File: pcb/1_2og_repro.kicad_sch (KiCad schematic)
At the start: 219 parts, among them J1 Pico EzMate, J2 USB_B_Mini, J3 Raw Header, J4 JST PH S3B, Q1 2N7002, SW1 MX_SW_solder, SW10 MX_SW_solder, SW11 MX_SW_solder, SW12 MX_SW_solder, SW13 MX_SW_solder, SW14 MX_SW_solder, SW15 MX_SW_solder, SW16 MX_SW_solder, SW17 MX_SW_solder, SW18 MX_SW_solder, SW19 MX_SW_solder, SW2 MX_SW_solder, SW20 MX_SW_solder, SW21 MX_SW_solder, SW22 MX_SW_solder, SW23 MX_SW_solder, SW24 MX_SW_solder, SW25 MX_SW_solder, SW26 MX_SW_solder, SW27 MX_SW_solder, SW28 MX_SW_solder, SW29 MX_SW_solder, SW3 MX_SW_solder, SW30 MX_SW_solder, SW31 MX_SW_solder, SW32 MX_SW_solder, SW33 MX_SW_solder, SW34 MX_SW_solder, SW35 MX_SW_solder, SW36 MX_SW_solder, SW37 MX_SW_solder, SW38 MX_SW_solder, SW39 MX_SW_solder, SW4 MX_SW_solder, SW40 MX_SW_solder, SW41 MX_SW_solder, SW42 MX_SW_solder, SW43 MX_SW_solder, SW44 MX_SW_solder, SW45 MX_SW_solder, SW46 MX_SW_solder, SW47 MX_SW_solder, SW48 MX_SW_solder, SW49 MX_SW_solder, SW5 MX_SW_solder, SW50 MX_SW_solder, SW51 MX_SW_solder, SW52 MX_SW_solder, SW53 MX_SW_solder, SW54 MX_SW_solder, SW55 MX_SW_solder, SW56 MX_SW_solder, SW57 MX_SW_solder, SW58 MX_SW_solder, SW59 MX_SW_solder, SW6 MX_SW_solder, SW60 MX_SW_solder, SW61 MX_SW_solder, SW62 MX_SW_solder, SW63 MX_SW_solder, SW64 MX_SW_solder, SW65 MX_SW_solder, SW66 MX_SW_solder, SW67 MX_SW_solder, SW68 MX_SW_solder, SW69 MX_SW_solder, SW7 MX_SW_solder, SW70 MX_SW_solder, SW71 MX_SW_solder, SW72 MX_SW_solder, SW73 MX_SW_solder, SW74 MX_SW_solder, SW75 MX_SW_solder, SW76 MX_SW_solder, SW77 MX_SW_solder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

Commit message: routing improvements
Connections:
- net COL10: now also U2.27 (PB14); no longer U2.26 (PB13)
- net COL11: now also U2.26 (PB13); no longer U2.25 (PB12)
- net COL12: now also U2.25 (PB12); no longer U2.28 (PB15)
- net COL9: now also U2.28 (PB15); no longer U2.27 (PB14)
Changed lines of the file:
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@@
     )
   )
-  (global_label "COL9" (shape input) (at 24.765 90.805 180) (fields_autoplaced)
+  (global_label "COL9" (shape input) (at 24.765 93.345 180) (fields_autoplaced)
     (effects (font (size 1.27 1.27)) (justify right))
-    (property "Intersheetrefs" "${INTERSHEET_REFS}" (at 17.0211 90.805 0)
+    (property "Intersheetrefs" "${INTERSHEET_REFS}" (at 17.0211 93.345 0)
       (effects (font (size 1.27 1.27)) (justify right) hide)
     )
@@
     )
   )
-  (global_label "COL10" (shape input) (at 24.765 88.265 180) (fields_autoplaced)
+  (global_label "COL10" (shape input) (at 24.765 90.805 180) (fields_autoplaced)
     (effects (font (size 1.27 1.27)) (justify right))
-    (property "Intersheetrefs" "${INTERSHEET_REFS}" (at 15.8116 88.265 0)
+    (property "Intersheetrefs" "${INTERSHEET_REFS}" (at 15.8116 90.805 0)
       (effects (font (size 1.27 1.27)) (justify right) hide)
     )
@@
     )
   )
-  (global_label "COL12" (shape input) (at 24.765 93.345 180) (fields_autoplaced)
-    (effects (font (size 1.27 1.27)) (justify right))
-    (property "Intersheetrefs" "${INTERSHEET_REFS}" (at 15.8116 93.345 0)
-      (effects (font (size 1.27 1.27)) (justify right) hide)
-    )
-  )
-  (global_label "COL11" (shape input) (at 24.765 85.725 180) (fields_autoplaced)
+  (global_label "COL12" (shape input) (at 24.765 85.725 180) (fields_autoplaced)
     (effects (font (size 1.27 1.27)) (justify right))
     (property "Intersheetrefs" "${INTERSHEET_REFS}" (at 15.8116 85.725 0)
       (effects (font (size 1.27 1.27)) (justify right) hide)
     )
+  )
+  (global_label "COL11" (shape input) (at 24.765 88.265 180) (fields_autoplaced)
+    (effects (font (size 1.27 1.27)) (justify right))
+    (property "Intersheetrefs" "${INTERSHEET_REFS}" (at 15.8116 88.265 0)
+      (effects (font (size 1.27 1.27)) (justify right) hide)
+    )

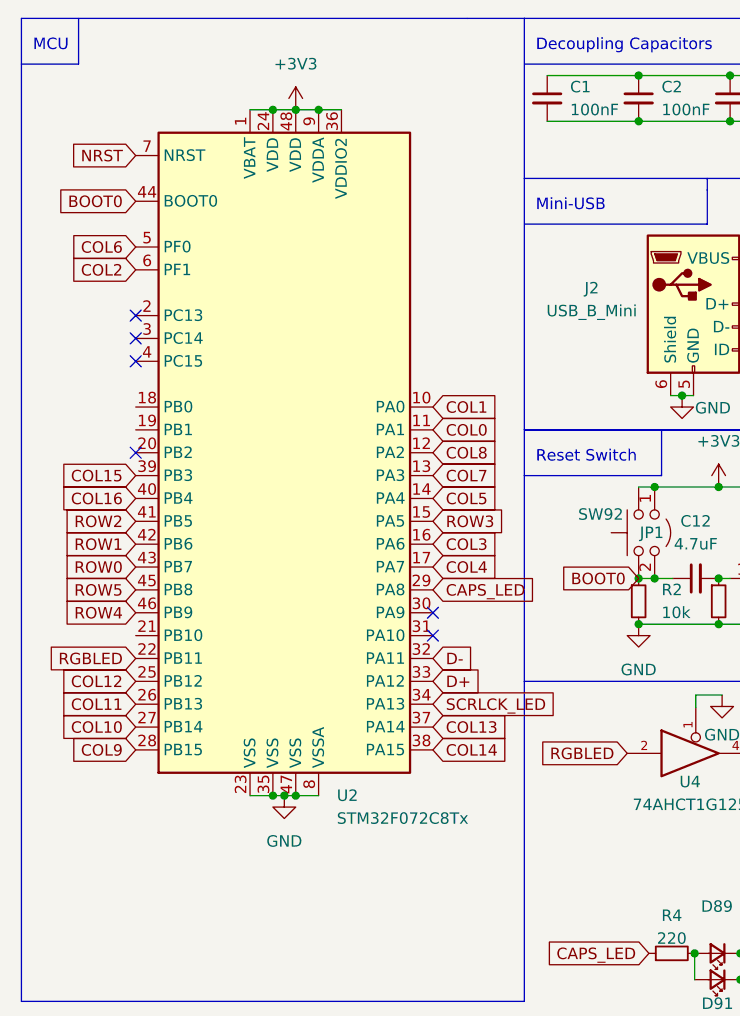
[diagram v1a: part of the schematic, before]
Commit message: fix 3v3 connections to mcu
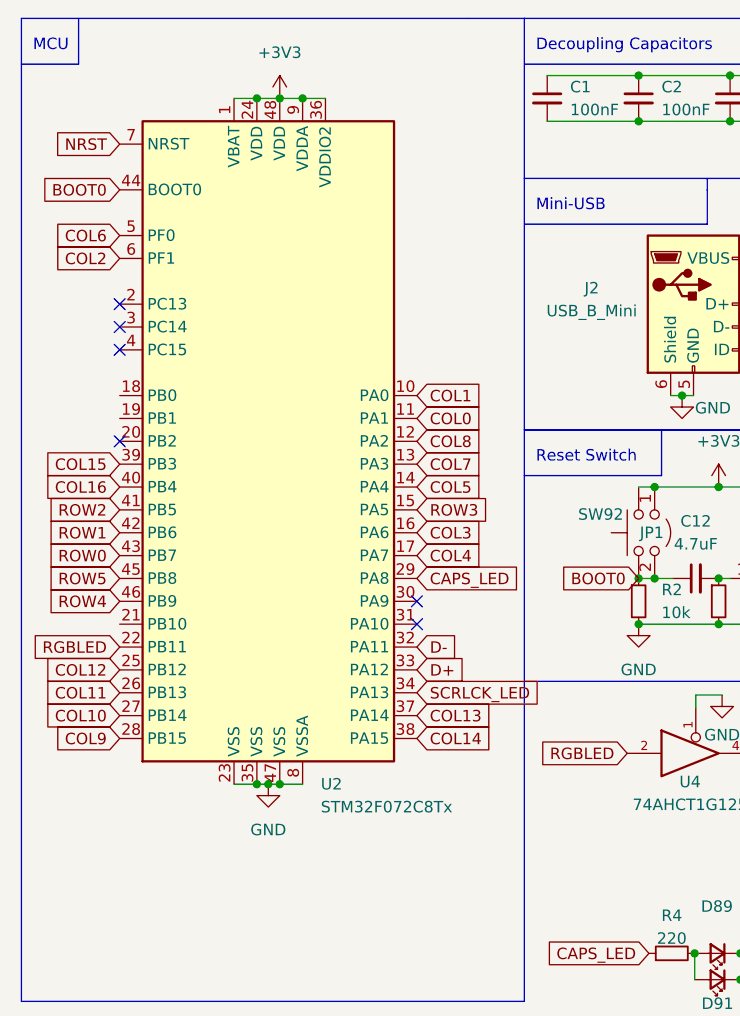
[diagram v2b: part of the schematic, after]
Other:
- moved on the sheet: U2

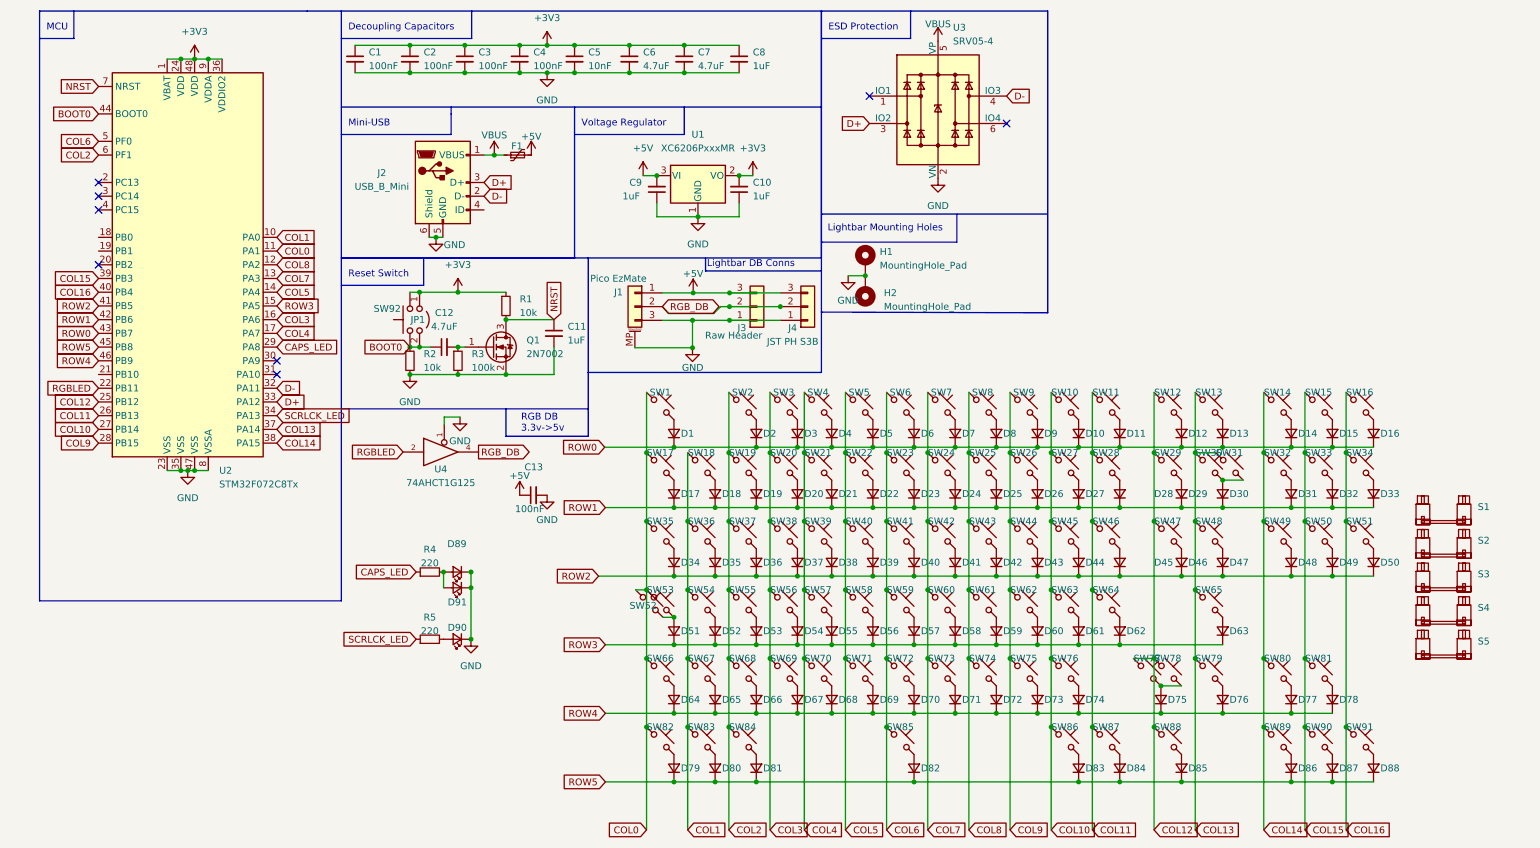
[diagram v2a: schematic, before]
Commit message: re-route pcb
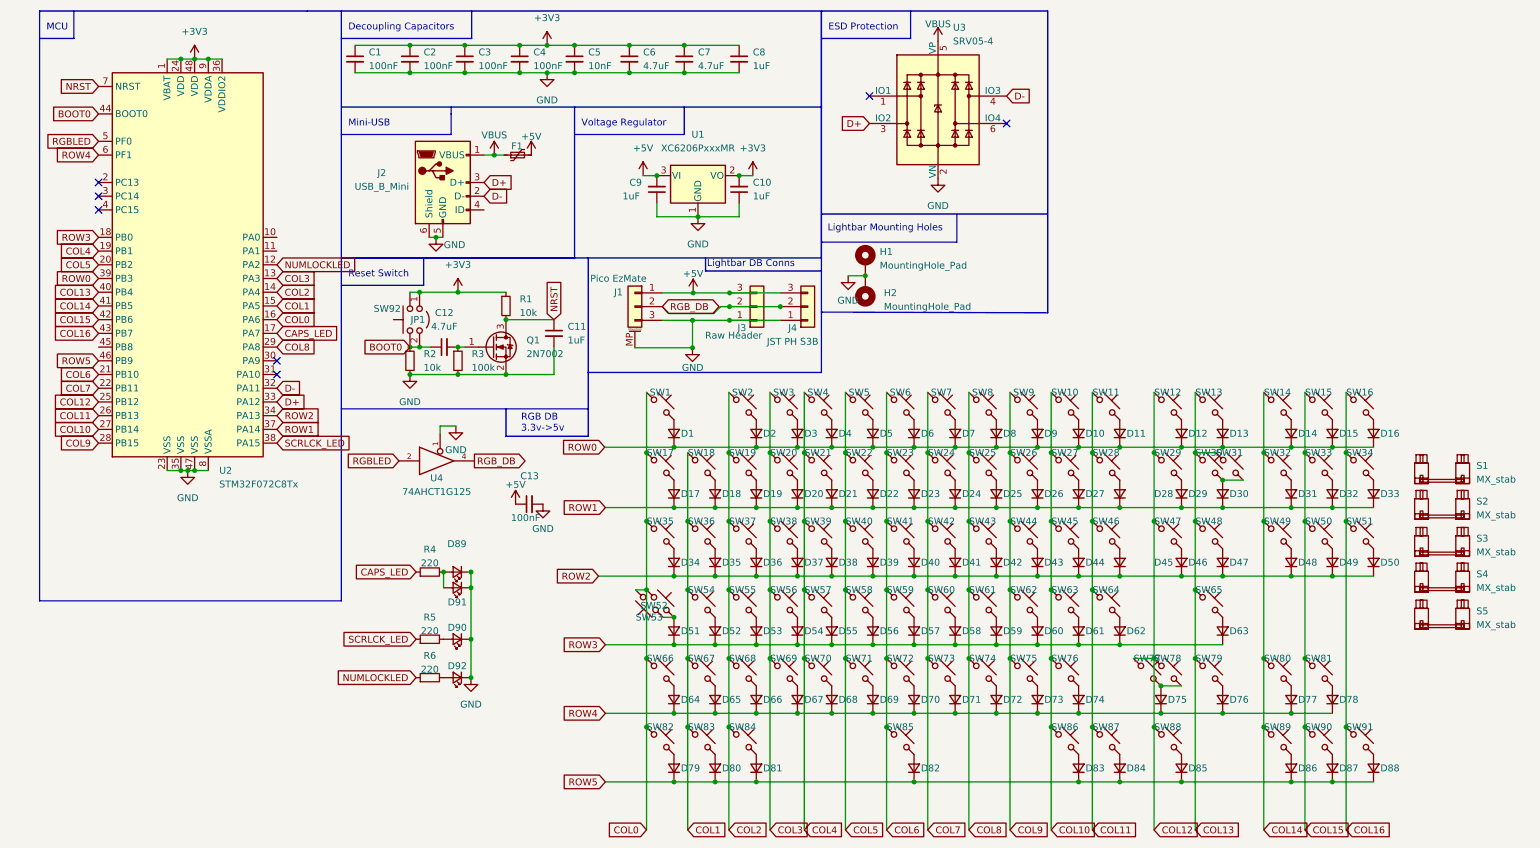
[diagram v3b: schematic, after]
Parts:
- added D92: LED_Small, marbastlib-mx:LED_MX_3mm, symbol Device:LED_Small
- added R6: 220, Resistor_SMD:R_0402_1005Metric, symbol Device:R_Small
- S2: footprint marbastlib-mx:STAB_MX_P_2.75u -> marbastlib-mx:STAB_MX_2.25u
- S4: footprint marbastlib-mx:STAB_MX_2.25u -> marbastlib-mx:STAB_MX_P_2.75u
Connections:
- net CAPS_LED: now also U2.17 (PA7); no longer U2.29 (PA8)
- net COL0: now also SW53.2, U2.16 (PA6); no longer SW53.1, U2.11 (PA1)
- net COL1: now also U2.15 (PA5); no longer U2.10 (PA0)
- net COL13: now also U2.40 (PB4); no longer U2.37 (PA14)
- net COL14: now also U2.41 (PB5); no longer U2.38 (PA15)
- net COL15: now also U2.42 (PB6); no longer U2.39 (PB3)
- net COL16: now also U2.43 (PB7); no longer U2.40 (PB4)
- net COL2: now also U2.14 (PA4); no longer U2.6 (PF1)
- net COL3: now also U2.13 (PA3); no longer U2.16 (PA6)
- net COL4: now also U2.19 (PB1); no longer U2.17 (PA7)
- net COL5: now also U2.20 (PB2); no longer U2.14 (PA4)
- net COL6: now also U2.21 (PB10); no longer U2.5 (PF0)
- net COL7: now also U2.22 (PB11); no longer U2.13 (PA3)
- net COL8: now also U2.29 (PA8); no longer U2.12 (PA2)
- net GND: now also D92.1 (K)
- net RGBLED: now also U2.5 (PF0); no longer U2.22 (PB11)
- net ROW0: now also U2.39 (PB3); no longer U2.43 (PB7)
- net ROW1: now also U2.37 (PA14); no longer U2.42 (PB6)
- net ROW2: now also U2.34 (PA13); no longer U2.41 (PB5)
- net ROW3: now also U2.18 (PB0); no longer U2.15 (PA5)
- net ROW4: now also U2.6 (PF1); no longer U2.46 (PB9)
- net ROW5: now also U2.46 (PB9); no longer U2.45 (PB8)
- net SCRLCK_LED: now also U2.38 (PA15); no longer U2.34 (PA13)
- net at D51.2 (A), SW52.2: now also SW53.1; no longer SW53.2
- new net: D92.2 (A), R6.2
- new net NUMLOCKLED: R6.1, U2.12 (PA2)
- no-connect marks 8 -> 7
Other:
- moved on the sheet: C13, SW52, SW53, U4

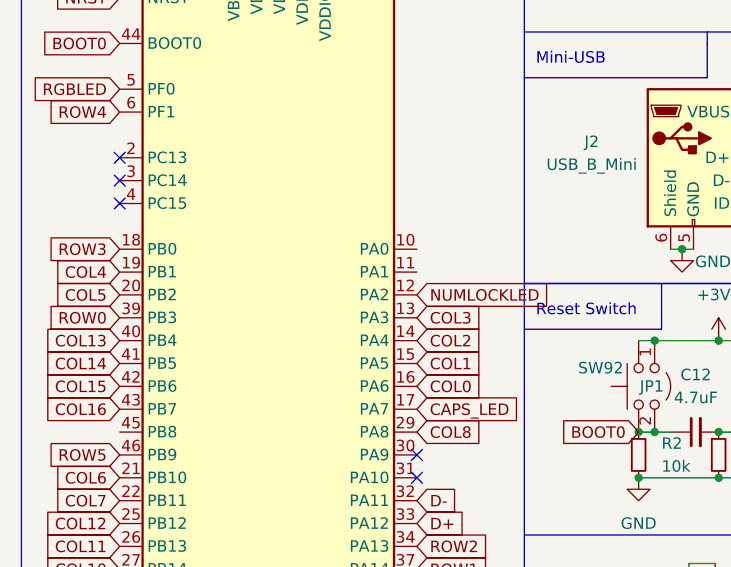
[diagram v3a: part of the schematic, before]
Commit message: do not use PB2 as column pin
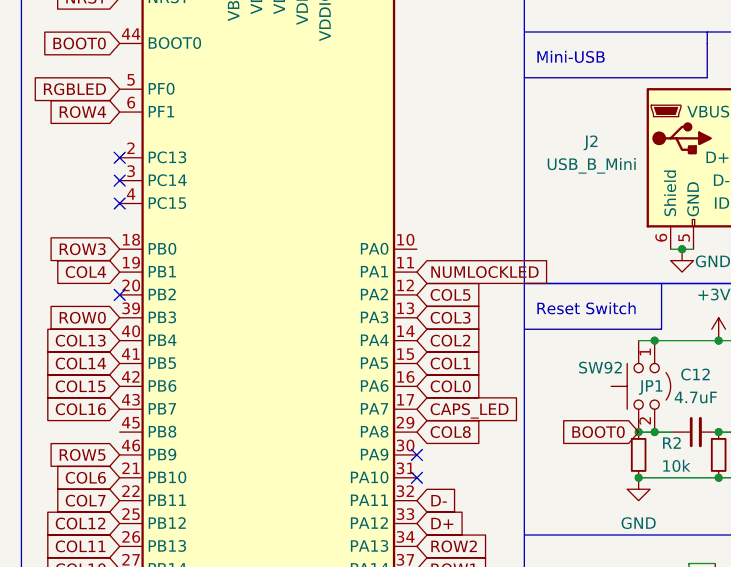
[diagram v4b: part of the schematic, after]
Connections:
- net COL5: now also U2.12 (PA2); no longer U2.20 (PB2)
- net NUMLOCKLED: now also U2.11 (PA1); no longer U2.12 (PA2)
- no-connect marks 7 -> 8
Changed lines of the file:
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@@
   (no_connect (at 165.735 27.813))
   (no_connect (at 22.987 43.815))
+  (no_connect (at 22.987 59.055))
   (no_connect (at 22.987 48.895))
   (no_connect (at 191.135 32.893))
@@
     )
   )
-  (global_label "COL5" (shape input) (at 22.987 59.055 180) (fields_autoplaced)
-    (effects (font (size 1.27 1.27)) (justify right))
-    (property "Intersheetrefs" "${INTERSHEET_REFS}" (at 15.2431 59.055 0)
-      (effects (font (size 1.27 1.27)) (justify right) hide)
+  (global_label "COL5" (shape input) (at 56.007 59.055 0) (fields_autoplaced)
+    (effects (font (size 1.27 1.27)) (justify left))
+    (property "Intersheetrefs" "${INTERSHEET_REFS}" (at 63.7509 59.055 0)
+      (effects (font (size 1.27 1.27)) (justify left) hide)
     )
   )
@@
     )
   )
-  (global_label "NUMLOCKLED" (shape input) (at 56.007 59.055 0) (fields_autoplaced)
-    (effects (font (size 1.27 1.27)) (justify left))
-    (property "Intersheetrefs" "${INTERSHEET_REFS}" (at 71.3709 59.055 0)
-      (effects (font (size 1.27 1.27)) (justify left) hide)
-    )
+  (global_label "NUMLOCKLED" (shape input) (at 56.007 56.515 0) (fields_autoplaced)
+    (effects (font (size 1.27 1.27)) (justify left))
+    (property "Intersheetrefs" "${INTERSHEET_REFS}" (at 71.3709 56.515 0)
+      (effects (font (size 1.27 1.27)) (justify left) hide)
+    )

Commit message: simplify
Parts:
- removed C12: 4.7uF, Capacitor_SMD:C_0402_1005Metric, symbol Device:C_Small
- removed Q1: 2N7002, Package_TO_SOT_SMD:SOT-23, symbol Transistor_FET:2N7002
- removed R5, R6: 220, Resistor_SMD:R_0402_1005Metric, symbol Device:R_Small
- removed SW92: SW_Push, Button_Switch_SMD:SW_SPST_TL3342, symbol Switch:SW_Push
- added J5: Foam, Connector_Wire:SolderWirePad_1x01_SMD_5x10mm, symbol Connector_Generic:Conn_01x01
- C11: value 1uF -> 100nF
- D90: footprint marbastlib-mx:LED_MX_3mm -> marbastlib-mx:LED_MX_3mm-ROT
- D91: footprint marbastlib-mx:LED_MX_3mm-ROT -> marbastlib-mx:LED_MX_3mm
- R2: value 10k -> 220
- R3: value 100k -> 220
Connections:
- net +3V3: no longer R1.1
- net BOOT0: now also R1.2; no longer R2.1
- net CAPS_LED: now also R2.1; no longer R4.1
- net GND: now also R1.1, J5.1 (Pin_1); no longer R2.2, R3.2
- net NRST: no longer R1.2
- net NUMLOCKLED: now also R4.1
- net SCRLCK_LED: now also R3.1
- net at D92.2 (A): now also R4.2
- net at D90.2 (A): now also D89.2 (A), R2.2
- new net: D91.2 (A), R3.2
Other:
- note added: "Reset Circuit"
- note removed: "Reset Switch"
- moved on the sheet: C11, JP1, R1
